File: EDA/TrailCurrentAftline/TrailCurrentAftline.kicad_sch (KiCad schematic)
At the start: 28 parts, among them IC1 SN65HVD230DR, J1 CAN_Bus, J2 Trailer_Input, U1 ESP32-C6-SuperMini, U2 Mini560, U3 TLP290, U4 TLP290, U5 TLP290, U6 TLP290

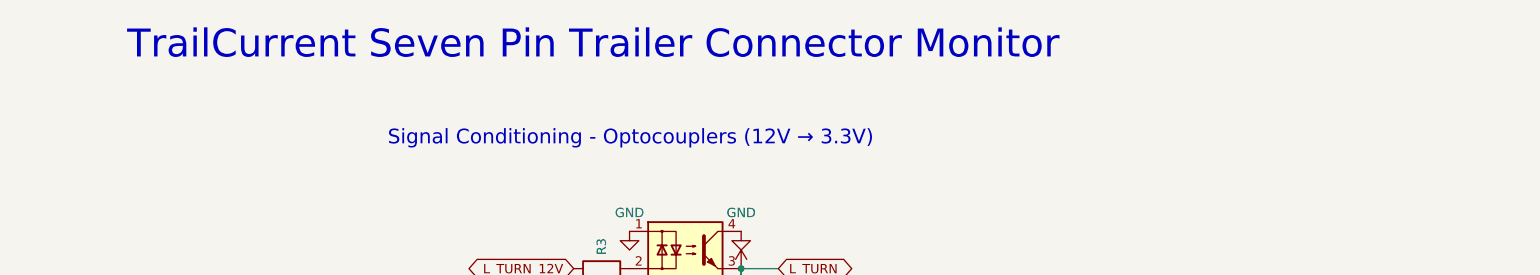
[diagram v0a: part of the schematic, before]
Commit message: Renamed to align with product names
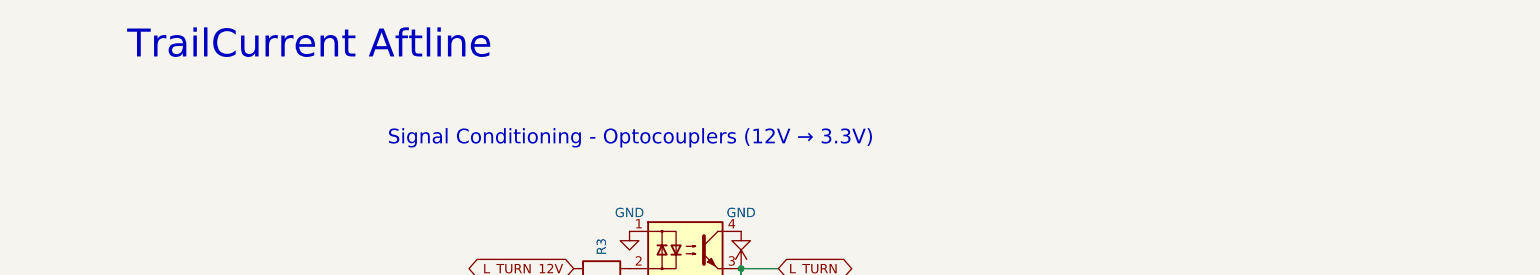
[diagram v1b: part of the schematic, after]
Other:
- note added: "TrailCurrent Aftline"
- note removed: "TrailCurrent Seven Pin Trailer Connector Monitor"
